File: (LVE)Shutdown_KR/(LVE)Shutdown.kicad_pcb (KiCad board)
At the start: 2 copper layers, 83.7 x 92.2 mm, 113 parts, among them J1 Conn_01x03_Pin, J10 Conn_BTN_Left, J11 Conn_BTN_Right, J12 Conn_BOTS_1, J13 Conn_BOTS_2, J14 Conn_Inertia, J15 Conn_HVD_INTL, J16 Conn_ACC_INTL, J17 Conn_TSMS, J18 Conn_discharge, J19 Conn_precharge, J2 Conn_01x06, J20 Conn_Power, J21 Conn_AIR 1, J22 Conn_AIR 2, J23 Conn_TSAL_OK, J24 IMD_LED, J27 AMS_LED, J3 Conn_01x06, J4 Conn_01x03, J5 IMD_RST, J6 AMS_RST, J8 Conn_BSPD, J9 Conn_BTN_Cockpit, K6 G5Q1A4DC12, K7 G5Q1A4DC12, Q1 2N7000, Q2 2N7000, Q3 2N7000, Q4 2N7000, U1 LM7805MPX/NOPB, U2 SN74AHC1G02DBVR, U6 MC74HC74ADG

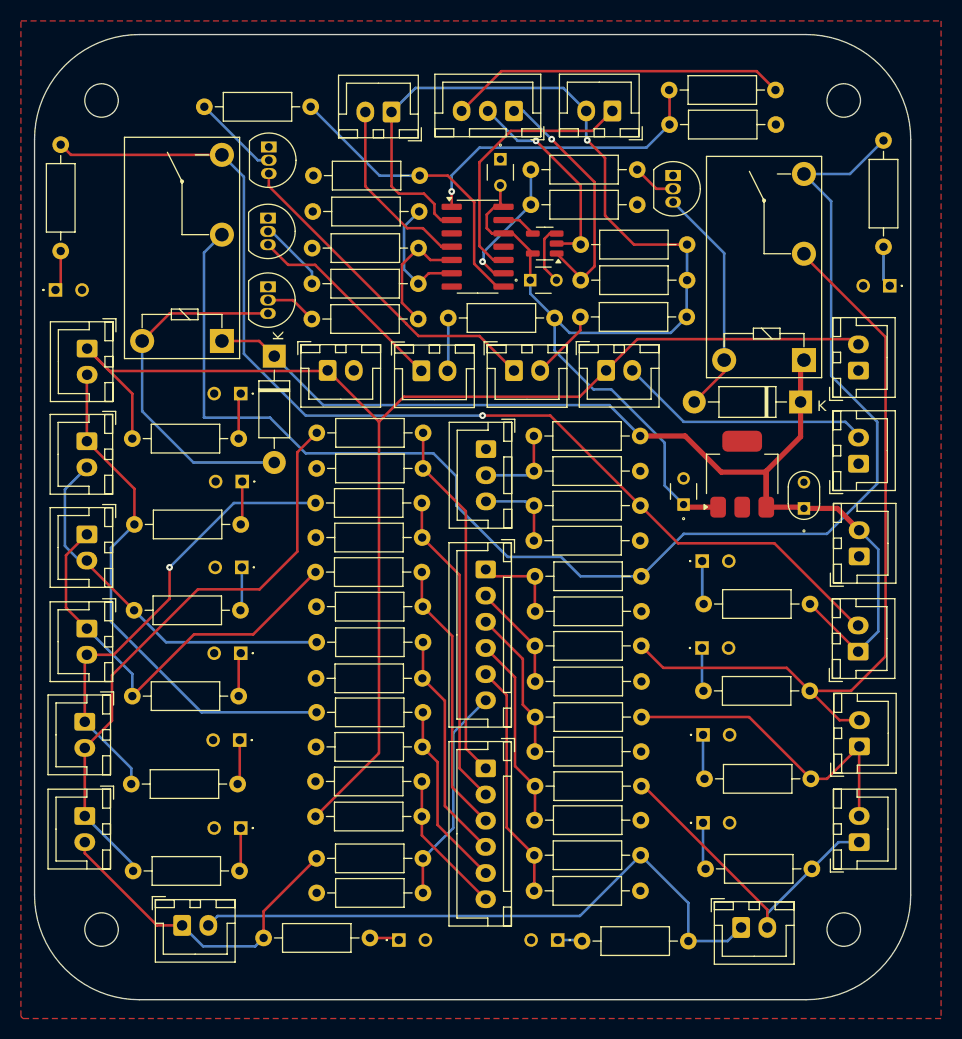
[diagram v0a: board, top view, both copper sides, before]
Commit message: Slave with SMD and no other fuses
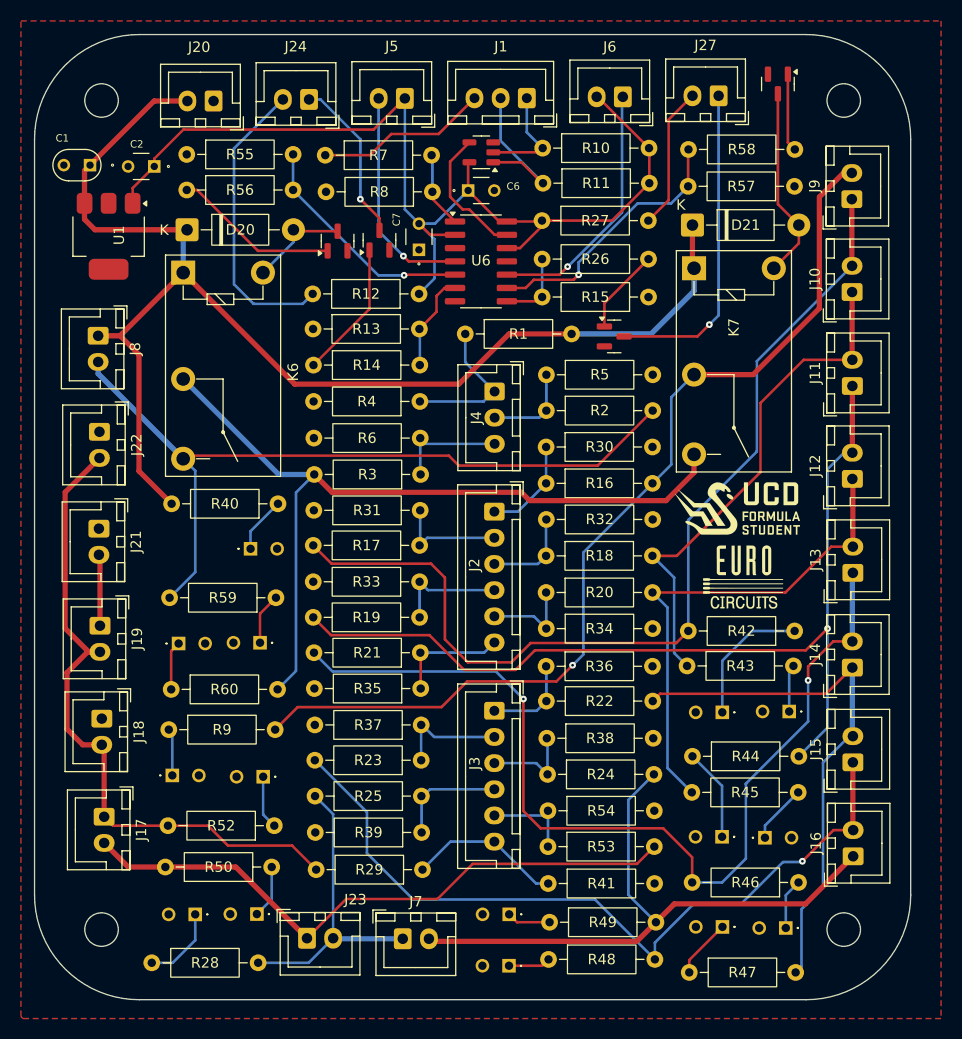
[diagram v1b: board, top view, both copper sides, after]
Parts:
- removed Q4: 2N7000, Package_TO_SOT_THT:TO-92_Inline
- added G***: LOGO, LOGO, F.Cu at (232.1, 77.6)
- added G***: LOGO, LOGO, F.Cu at (232.7, 84.3)
- added J7: HV_SENSE_INTL, Connector_JST:JST_XH_B2B-XH-A_1x02_P2.50mm_Vertical, F.Cu at (200.2, 118.7)
- added LED15: LTL-1CHG, Kicad_Libraries:LTL1CHG, F.Cu at (180.3, 116.3)
- added Q5: 2N7002, Package_TO_SOT_SMD:SOT-23, F.Cu at (193.9, 52.0)
- added R28: 10k, Resistor_THT:R_Axial_DIN0207_L6.3mm_D2.5mm_P10.16mm_Horizontal, F.Cu at (176.2, 121.0)
- added R29: 27k, Resistor_THT:R_Axial_DIN0207_L6.3mm_D2.5mm_P10.16mm_Horizontal, F.Cu at (202.1, 112.1)
- added R41: 10k, Resistor_THT:R_Axial_DIN0207_L6.3mm_D2.5mm_P10.16mm_Horizontal, F.Cu at (214.1, 113.4)
- C1: footprint FA14_Capacitor:FA14X7R1H224KNU00 -> Kicad_Libraries:FA14X7R1H224KNU00
- C2, C6, C7: footprint FA14_Capacitor:FA18X7R1H104KNU00 -> Kicad_Libraries:FA18X7R1H104KNU00
- LED1, LED10, LED11, LED12, LED13, LED14, LED2, LED3, LED4, LED5, LED6, LED7, LED8, LED9: footprint LTL1CHG:LTL1CHG -> Kicad_Libraries:LTL1CHG
- Q1, Q2, Q3: value 2N7000 -> 2N7002; footprint Package_TO_SOT_THT:TO-92_Inline -> Package_TO_SOT_SMD:SOT-23
- moved R60 80.1 mm to (178.1, 94.9), turned to 0 degrees
- moved J16 79.4 mm to (243.2, 110.8), turned to 90 degrees
- moved J8 78.6 mm to (171.1, 61.1), turned to -90 degrees
- moved J13 77.0 mm to (243.2, 83.7), turned to 90 degrees
- moved J12 76.9 mm to (243.1, 74.8), turned to 90 degrees
- moved LED2 76.1 mm to (178.8, 90.5), turned to 0 degrees
- moved C1 75.7 mm to (170.3, 44.8), turned to 180 degrees
- moved J20 75.5 mm to (182.1, 38.6), turned to 180 degrees
- moved J15 74.3 mm to (243.2, 101.8), turned to 90 degrees
- moved J14 73.5 mm to (243.1, 92.8), turned to 90 degrees
- moved J21 72.8 mm to (171.2, 79.5), turned to -90 degrees
- moved J22 72.7 mm to (171.2, 70.2), turned to -90 degrees
- moved U1 64.7 mm to (172.1, 51.6), turned to -90 degrees
- moved C2 60.0 mm to (176.4, 44.9), turned to 180 degrees
- moved J19 54.2 mm to (171.2, 88.8), turned to -90 degrees
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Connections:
- net COCKPIT_IN renamed B
- J1 pad 1: Multi purpose enable -> Discharge enable
- J1 pad 2: Discharge enable -> Multi purpose enable
- J16 pad 1: Net-(J15-Pin_1) -> Net-(J16-Pin_1)
- J16 pad 2: Net-(J16-Pin_2) -> Net-(J15-Pin_1)
- J18 pad 1: Net-(J17-Pin_1) -> GLVS-
- J18 pad 2: GLVS- -> Net-(J17-Pin_1)
- J19 pad 1: Net-(J17-Pin_1) -> Net-(J19-Pin_1)
- J19 pad 2: Net-(J19-Pin_2) -> Net-(J17-Pin_1)
- J21 pad 2: Net-(J19-Pin_2) -> Net-(J19-Pin_1)
- J23 pad 2: Net-(J16-Pin_2) -> Net-(J23-Pin_2)
- J4 pad 1: GLVS- -> Net-(J4-Pin_1)
- J8 pad 2: A -> IMD_IN
- K6 pad 2: AMS_IN -> A
- K6 pad 3: A -> IMD_IN
- K7 pad 3: AMS_IN -> A
- Q1 pad 1: GLVS- -> Net-(Q1-G)
- Q1 pad 2: Net-(Q1-G) -> GLVS-
- Q1 pad 3: Net-(D20-A) -> Net-(D21-A)
- Q2 pad 1: GLVS- -> Net-(Q2-G)
- Q2 pad 2: Net-(Q2-G) -> GLVS-
- Q2 pad 3: Net-(D21-A) -> IMD_LED-
- Q3 pad 1: GLVS- -> Net-(Q3-G)
- Q3 pad 2: Net-(Q3-G) -> GLVS-
- Q3 pad 3: IMD_LED- -> AMS_LED-
- R1 pad 1: Net-(J4-Pin_2) -> Net-(J4-Pin_1)
- R14 pad 1: Net-(Q3-G) -> Net-(Q2-G)
- R16 pad 1: Net-(J2-Pin_2) -> Net-(J2-Pin_1)
- R17 pad 1: Net-(J2-Pin_3) -> Net-(J2-Pin_2)
- R18 pad 1: Net-(J2-Pin_4) -> Net-(J2-Pin_3)
- R19 pad 1: Net-(J2-Pin_5) -> Net-(J2-Pin_4)
- R2 pad 1: Net-(J4-Pin_3) -> Net-(J4-Pin_2)
- R2 pad 2: A -> IMD_IN
- R20 pad 1: Net-(J2-Pin_6) -> Net-(J2-Pin_5)
- R21 pad 1: Net-(J3-Pin_1) -> Net-(J2-Pin_6)
- R22 pad 1: Net-(J3-Pin_2) -> Net-(J3-Pin_1)
- R23 pad 1: Net-(J3-Pin_3) -> Net-(J3-Pin_2)
- R24 pad 1: Net-(J3-Pin_4) -> Net-(J3-Pin_3)
- R24 pad 2: Net-(J16-Pin_2) -> Net-(J16-Pin_1)
- R25 pad 1: Net-(J3-Pin_5) -> Net-(J3-Pin_4)
- R25 pad 2: Net-(J17-Pin_2) -> Net-(J23-Pin_2)
- R26 pad 1: Net-(Q4-G) -> Net-(Q3-G)
- R3 pad 1: Net-(J2-Pin_1) -> Net-(J4-Pin_3)
- R3 pad 2: AMS_IN -> A
- R30 pad 1: Net-(J2-Pin_2) -> Net-(J2-Pin_1)
- R31 pad 1: Net-(J2-Pin_3) -> Net-(J2-Pin_2)
- R32 pad 1: Net-(J2-Pin_4) -> Net-(J2-Pin_3)
- R33 pad 1: Net-(J2-Pin_5) -> Net-(J2-Pin_4)
- R34 pad 1: Net-(J2-Pin_6) -> Net-(J2-Pin_5)
- R35 pad 1: Net-(J3-Pin_1) -> Net-(J2-Pin_6)
- R36 pad 1: Net-(J3-Pin_2) -> Net-(J3-Pin_1)
- R37 pad 1: Net-(J3-Pin_3) -> Net-(J3-Pin_2)
- R38 pad 1: Net-(J3-Pin_4) -> Net-(J3-Pin_3)
- R39 pad 1: Net-(J3-Pin_5) -> Net-(J3-Pin_4)
- R4 pad 1: Net-(J4-Pin_2) -> Net-(J4-Pin_1)
- R49 pad 2: Net-(J16-Pin_2) -> Net-(J16-Pin_1)
- R5 pad 1: Net-(J4-Pin_3) -> Net-(J4-Pin_2)
- R53 pad 1: Net-(J3-Pin_6) -> Net-(J3-Pin_5)
- R53 pad 2: Net-(J17-Pin_1) -> Net-(J17-Pin_2)
- R54 pad 1: Net-(J3-Pin_6) -> Net-(J3-Pin_5)
- R56 pad 1: Net-(Q1-G) -> Net-(Q5-G)
- R58 pad 1: Net-(Q2-G) -> Net-(Q1-G)
- R59 pad 2: A -> IMD_IN
- R6 pad 1: Net-(J2-Pin_1) -> Net-(J4-Pin_3)
- R60 pad 2: AMS_IN -> A
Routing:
- net AMS_IN: track 135.5 -> 0.00 mm
- net IMD_IN: track 0.00 -> 74.9 mm
- net Net-(J17-Pin_1): track 131.1 -> 64.5 mm
- net Net-(J10-Pin_2): track 31.2 -> 92.9 mm
- net Net-(J16-Pin_1): track 0.00 -> 60.2 mm
- net Net-(J16-Pin_2): track 36.4 -> 0.00 mm
- net Net-(J13-Pin_1): track 56.4 -> 92.0 mm, vias 0 -> 2
- net Net-(J15-Pin_1): track 41.3 -> 74.1 mm, vias 0 -> 1
- net Net-(J11-Pin_1): track 59.7 -> 90.8 mm, vias 0 -> 1
- net Net-(J23-Pin_2): track 0.00 -> 29.1 mm
- net A: track 105.2 -> 78.4 mm, vias 1 -> 0
- net Net-(J3-Pin_1): track 34.5 -> 8.69 mm
- net Net-(D20-A): track 34.5 -> 9.58 mm
- net Net-(J19-Pin_2): track 24.2 -> 0.00 mm
- net IMD_LED+: track 5.08 -> 28.3 mm
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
